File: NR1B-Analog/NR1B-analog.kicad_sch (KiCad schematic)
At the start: 64 parts, among them J8 Conn_01x04_Male, U1 DAC11001BPFBR, U10 LT3042MPMSE-PBF, U11 LDK320ADU120R, U12 20K, U13 OPA2189IDR, U14 DAC11001BPFBR, U2 ADR444ARZ, U3 OPA189IDGKT, U4 OPA2189IDR, U7 LT3093EMSE-PBF, U8 20K, U9 10K

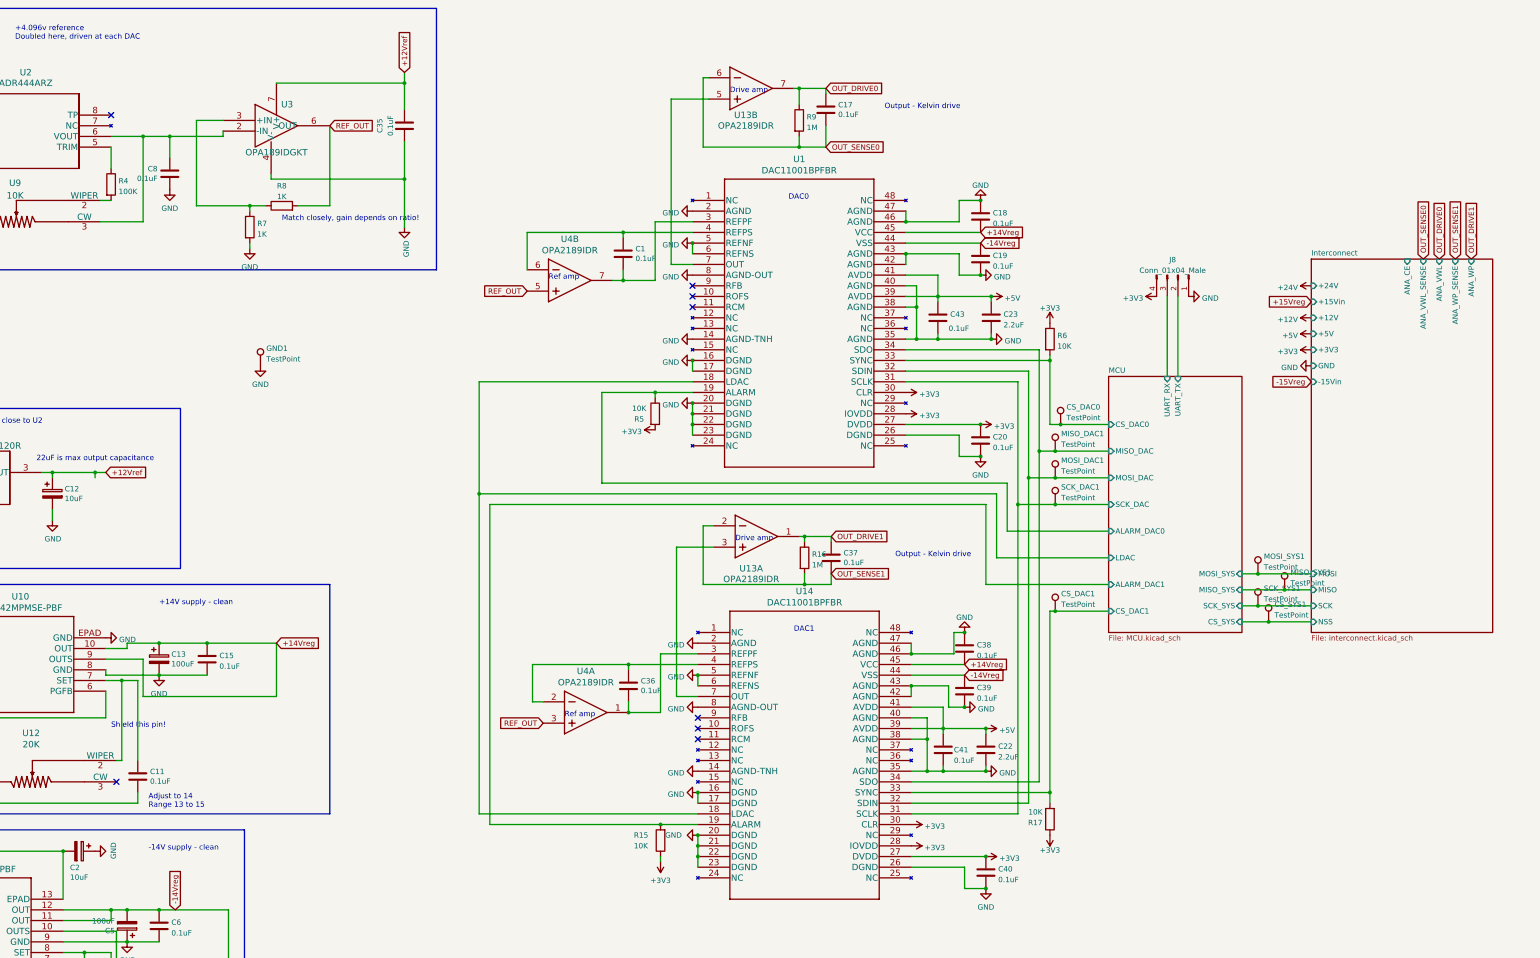
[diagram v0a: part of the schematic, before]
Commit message: Added ADC for voltage reading
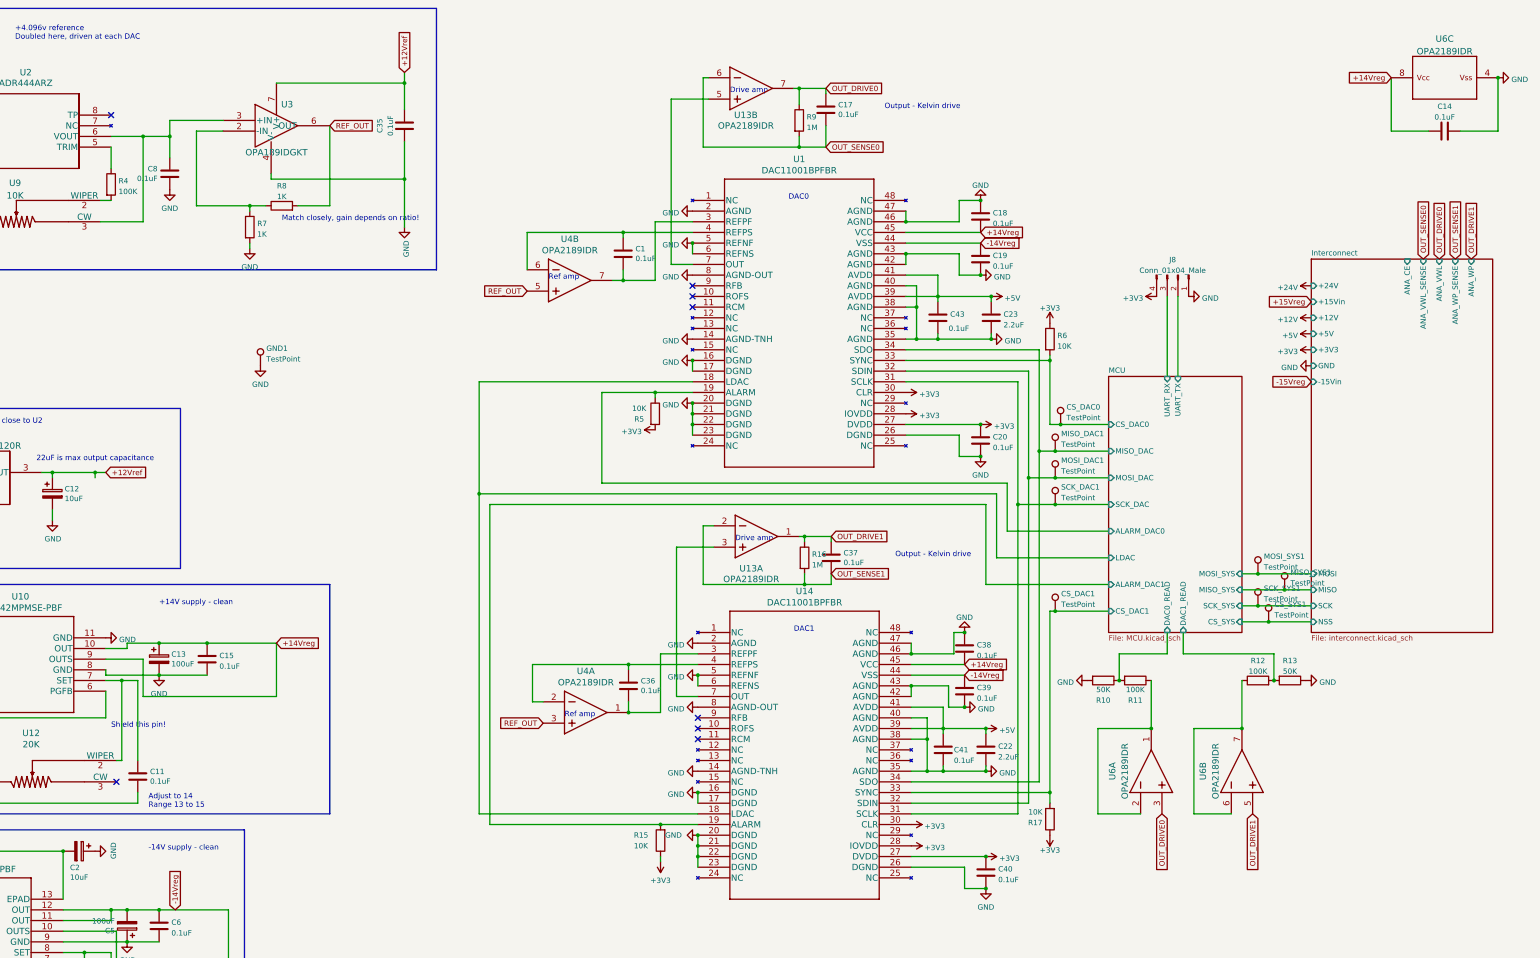
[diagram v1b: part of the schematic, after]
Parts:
- added C14: 0.1uF, Capacitor_SMD:C_0603_1608Metric, symbol Device:C
- added R10, R13: 50K, Resistor_SMD:R_0603_1608Metric, symbol Device:R
- added R11, R12: 100K, Resistor_SMD:R_0603_1608Metric, symbol Device:R
- added U6: OPA2189IDR, Package_SO:VSSOP-8_3.0x3.0mm_P0.65mm, symbol 2022-06-28_19-20-58:OPA2189IDR
- U1, U14: footprint PQFP48_DAC11001_TEX -> Package_QFP:TQFP-48_7x7mm_P0.5mm
- U10: footprint LT3042MPMSE-PBF_ADI -> Package_SO:MSOP-10-1EP_3x3mm_P0.5mm_EP1.68x1.88mm
- U11: footprint SOT-89_STM -> Package_TO_SOT_SMD:SOT-89-3
- U12, U8, U9: footprint SOT_3224J_BRN -> 3224J-1-103E:3224J-1-103E
- U13, U4: footprint D0008A_N -> Package_SO:VSSOP-8_3.0x3.0mm_P0.65mm
- U2: footprint R_8_ADI -> Package_SO:SO-8_3.9x4.9mm_P1.27mm
- U3: footprint DGK8_TEX -> Package_SO:VSSOP-8_3.0x3.0mm_P0.65mm
- U7: footprint LT3093EMSE-PBF_ADI -> Package_SO:MSOP-12-1EP_3x4mm_P0.65mm_EP1.65x2.85mm
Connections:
- net +14Vreg: now also C14.1, U6.8 (V+)
- net GND: now also U10.11 (GND), C14.2, R10.2, R13.1, U6.4 (V-); no longer U10.EPAD (GND)
- net OUT_DRIVE0: now also U6.3 (IN+)
- net OUT_DRIVE1: now also U6.5 (IN+)
- net at C8.1, U2.6 (VOUT), U9.3 (CW): now also U3.3 (+IN); no longer U3.2 (-IN)
- net at R7.1, R8.1: now also U3.2 (-IN); no longer U3.3 (+IN)
- new net: R11.1, U6.1 (OUT), U6.2 (IN-)
- new net: R12.1, U6.6 (IN-), U6.7 (OUT)
- new net MCU/DAC0_READ: R10.1, R11.2
- new net MCU/DAC1_READ: R12.2, R13.2
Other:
- sheet MCU ports: added DAC0_READ, DAC1_READ; removed none

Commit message: Fixed symbol libs, see notes from July 25 on PCB and schema
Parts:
- removed C41, C43: 0.1uF, Capacitor_SMD:C_0603_1608Metric, symbol Device:C
- added R18, R19: 47, Resistor_SMD:R_0603_1608Metric, symbol Device:R
- J8: value Conn_01x04_Male -> UART
- R10, R13: value 50K -> 47K
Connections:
- net MCU/DAC1_READ: now also R12.1; no longer R12.2
- net MCU/MISO_DAC: now also R18.2, R19.1; no longer U1.34 (SDO), U14.34 (SDO)
- net at U6.6 (IN-), U6.7 (OUT): now also R12.2; no longer R12.1
- new net: R18.1, U1.34 (SDO)
- new net: R19.2, U14.34 (SDO)
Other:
- sheet Interconnect ports: added ACK, ERROR; removed ANA_CE
- sheet MCU ports: added ACK, ERROR; removed none
- note added: "7/25/2022"
- note added: "ADC amp"
- note added: "Adjust to -14 range -13 to -15"
- note added: "Match R7 and R8 closely, gain depends on ratio!"
- note added: "NR1B-Analog"
- note added: "v1.0"
- note removed: "Adjust for -14 exactly range -13 to -15"
- note removed: "Match closely, gain depends on ratio!"
- note removed: "Shield this pin!"
- moved on the sheet: C10, C12, C14, C22, C23, CS_DAC1, CS_SYS1, GND1, MISO_SYS1, MOSI_SYS1, R10, R11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

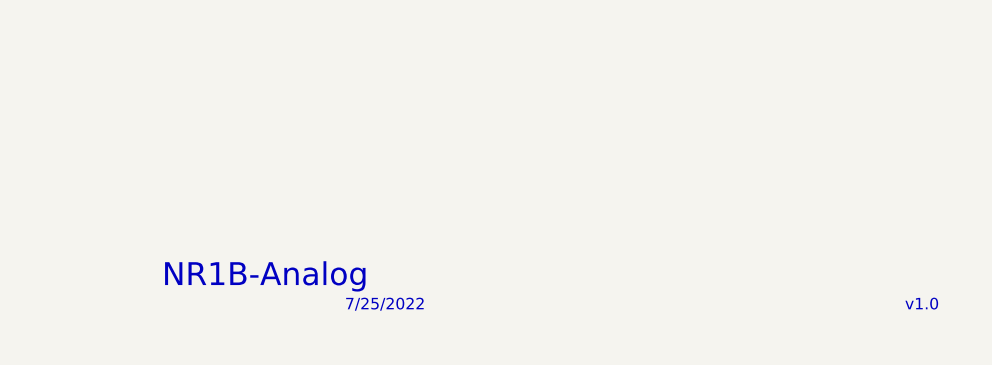
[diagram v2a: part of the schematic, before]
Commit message: Labeled sheets, adjusted pot location
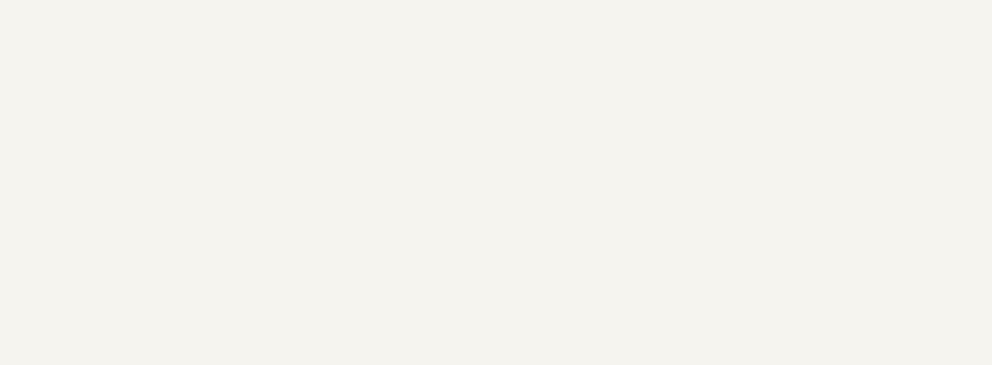
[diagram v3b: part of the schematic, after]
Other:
- note removed: "7/25/2022"
- note removed: "NR1B-Analog"
- note removed: "v1.0"
- company: (none) -> University of Dallas
- title: (none) -> NR1B-Analog
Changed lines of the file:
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@@
 (kicad_sch (version 20211123) (generator eeschema)
   (paper "USLedger")
+  (title_block
+    (title "NR1B-Analog")
+    (date "2022-07-26")
+    (rev "v1.0")
+    (company "University of Dallas")
+    (comment 1 "Isaac Kelly")
+  )
   (junction (at 25.4 227.33) (diameter 0) (color 0 0 0 0)
   )
@@
     (effects (font (size 1.27 1.27)) (justify left bottom))
   )
-  (text "v1.0" (at 403.86 262.89 0)
-    (effects (font (size 1.27 1.27)) (justify left bottom))
-  )
   (text "Adjust to 14\nRange 13 to 15" (at 91.44 203.2 0)
     (effects (font (size 1.27 1.27)) (justify left bottom))
@@
     (effects (font (size 1.27 1.27)) (justify left bottom))
   )
-  (text "7/25/2022" (at 341.63 262.89 0)
-    (effects (font (size 1.27 1.27)) (justify left bottom))
-  )
   (text "Ref amp" (at 186.69 77.47 0)
     (effects (font (size 1.27 1.27)) (justify left bottom))
@@
     (effects (font (size 1.27 1.27)) (justify left bottom))
   )
-  (text "NR1B-Analog" (at 321.31 260.35 0)
-    (effects (font (size 2.54 2.54)) (justify left bottom))
-  )
   (text "Adjust to -14\nrange -13 to -15" (at 83.82 262.89 0)

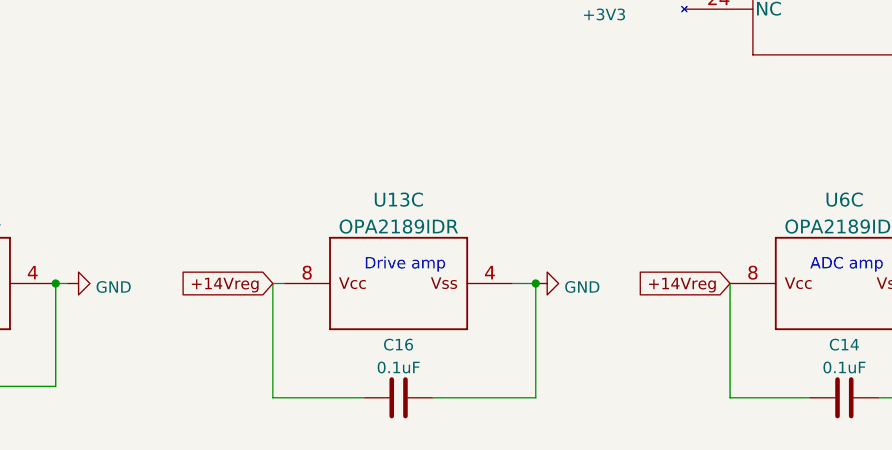
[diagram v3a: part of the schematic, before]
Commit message: 12v supply to dual op-amps
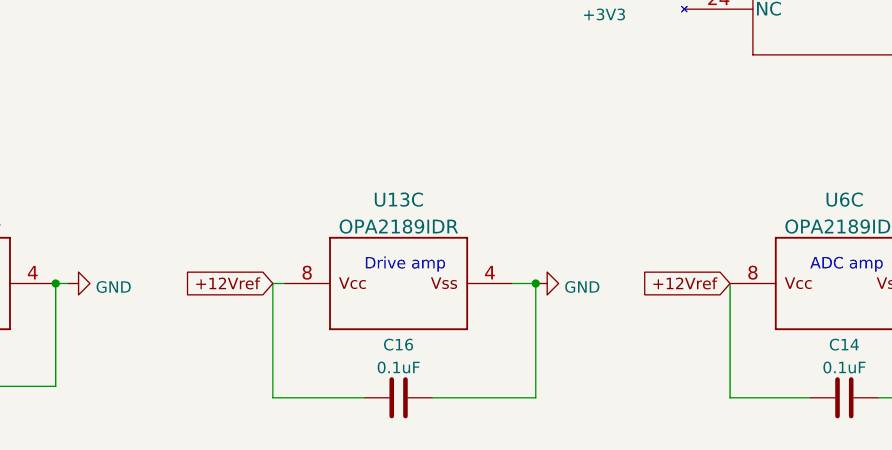
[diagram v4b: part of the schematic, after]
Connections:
- net +12Vref: now also C14.1, C16.1, U13.8 (V+), U6.8 (V+)
- net +14Vreg: no longer C14.1, C16.1, U13.8 (V+), U6.8 (V+)
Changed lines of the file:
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@@
-    )
-  )
-  (global_label "+14Vreg" (shape input) (at 176.53 250.19 180) (fields_autoplaced)
-    (effects (font (size 1.27 1.27)) (justify right))
-    (property "Intersheet References" "${INTERSHEET_REFS}" (id 0) (at 166.102 250.2694 0)
-      (effects (font (size 1.27 1.27)) (justify right) hide)
     )
   )
@@
     (property "Intersheet References" "${INTERSHEET_REFS}" (id 0) (at 266.9075 45.6406 0)
       (effects (font (size 1.27 1.27)) (justify left) hide)
+    )
+  )
+  (global_label "+12Vref" (shape input) (at 227.33 250.19 180) (fields_autoplaced)
+    (effects (font (size 1.27 1.27)) (justify right))
+    (property "Intersheet References" "${INTERSHEET_REFS}" (id 0) (at 217.3253 250.1106 0)
+      (effects (font (size 1.27 1.27)) (justify right) hide)
     )
   )
@@
     (property "Intersheet References" "${INTERSHEET_REFS}" (id 0) (at 145.048 40.5606 0)
       (effects (font (size 1.27 1.27)) (justify left) hide)
-    )
-  )
-  (global_label "+14Vreg" (shape input) (at 227.33 250.19 180) (fields_autoplaced)
-    (effects (font (size 1.27 1.27)) (justify right))
-    (property "Intersheet References" "${INTERSHEET_REFS}" (id 0) (at 216.902 250.1106 0)
-      (effects (font (size 1.27 1.27)) (justify right) hide)
     )
   )
@@
     )
   )
+  (global_label "+12Vref" (shape input) (at 176.53 250.19 180) (fields_autoplaced)
+    (effects (font (size 1.27 1.27)) (justify right))
+    (property "Intersheet References" "${INTERSHEET_REFS}" (id 0) (at 166.5253 250.1106 0)
+      (effects (font (size 1.27 1.27)) (justify right) hide)
+    )
+  )

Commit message: BOM, fiducials
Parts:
- added FID1, FID2, FID3: Fiducial, Fiducial:Fiducial_0.5mm_Mask1.5mm, symbol Mechanical:Fiducial
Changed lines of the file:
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@@
     (pin "1")
+  )
+  (symbol (lib_id "Mechanical:Fiducial") (at 369.57 33.02 0) (unit 1)
+    (in_bom yes) (on_board yes) (fields_autoplaced)
+    (property "Reference" "FID2" (id 0) (at 371.729 32.1853 0)
+      (effects (font (size 1.27 1.27)) (justify left))
+    )
+    (property "Value" "Fiducial" (id 1) (at 371.729 34.7222 0)
+      (effects (font (size 1.27 1.27)) (justify left))
+    )
+    (property "Footprint" "Fiducial:Fiducial_0.5mm_Mask1.5mm" (id 2) (at 369.57 33.02 0)
+      (effects (font (size 1.27 1.27)) hide)
+    )
+    (property "Datasheet" "~" (id 3) (at 369.57 33.02 0)
+      (effects (font (size 1.27 1.27)) hide)
+    )
   )
   (symbol (lib_id "Device:C") (at 289.56 115.57 0) (unit 1)
@@
     (pin "8")
   )
+  (symbol (lib_id "Mechanical:Fiducial") (at 369.57 22.86 0) (unit 1)
+    (in_bom yes) (on_board yes) (fields_autoplaced)
+    (property "Reference" "FID1" (id 0) (at 371.729 22.0253 0)
+      (effects (font (size 1.27 1.27)) (justify left))
+    )
+    (property "Value" "Fiducial" (id 1) (at 371.729 24.5622 0)
+      (effects (font (size 1.27 1.27)) (justify left))
+    )
+    (property "Footprint" "Fiducial:Fiducial_0.5mm_Mask1.5mm" (id 2) (at 369.57 22.86 0)
+      (effects (font (size 1.27 1.27)) hide)
+    )
+    (property "Datasheet" "~" (id 3) (at 369.57 22.86 0)
+      (effects (font (size 1.27 1.27)) hide)
+    )
+  )
   (symbol (lib_id "Device:C") (at 289.56 62.23 0) (unit 1)
     (in_bom yes) (on_board yes) (fields_autoplaced)
@@
     )
     (pin "1")
+  )
+  (symbol (lib_id "Mechanical:Fiducial") (at 369.57 43.18 0) (unit 1)
+    (in_bom yes) (on_board yes) (fields_autoplaced)
+    (property "Reference" "FID3" (id 0) (at 371.729 42.3453 0)
+      (effects (font (size 1.27 1.27)) (justify left))
+    )
+    (property "Value" "Fiducial" (id 1) (at 371.729 44.8822 0)
+      (effects (font (size 1.27 1.27)) (justify left))
+    )
+    (property "Footprint" "Fiducial:Fiducial_0.5mm_Mask1.5mm" (id 2) (at 369.57 43.18 0)
+      (effects (font (size 1.27 1.27)) hide)
+    )
+    (property "Datasheet" "~" (id 3) (at 369.57 43.18 0)
+      (effects (font (size 1.27 1.27)) hide)
+    )
   )
   (symbol (lib_id "power:GND") (at 96.52 55.88 0) (unit 1)
@@
       (reference "FB3") (unit 1) (value "FerriteBead") (footprint "Inductor_SMD:L_0805_2012Metric")
     )
+    (path "/a156e368-5eaa-4055-885b-4dc6a9421257"
+      (reference "FID1") (unit 1) (value "Fiducial") (footprint "Fiducial:Fiducial_0.5mm_Mask1.5mm")
+    )
+    (path "/75a6e213-de52-4f99-93dc-2e97dfd7dafa"
+      (reference "FID2") (unit 1) (value "Fiducial") (footprint "Fiducial:Fiducial_0.5mm_Mask1.5mm")
+    )
+    (path "/abf288d1-2057-41b6-a678-d28b983d7fd8"
+      (reference "FID3") (unit 1) (value "Fiducial") (footprint "Fiducial:Fiducial_0.5mm_Mask1.5mm")
+    )
     (path "/04181750-5cf6-4122-b89d-e16ab9ca9019"

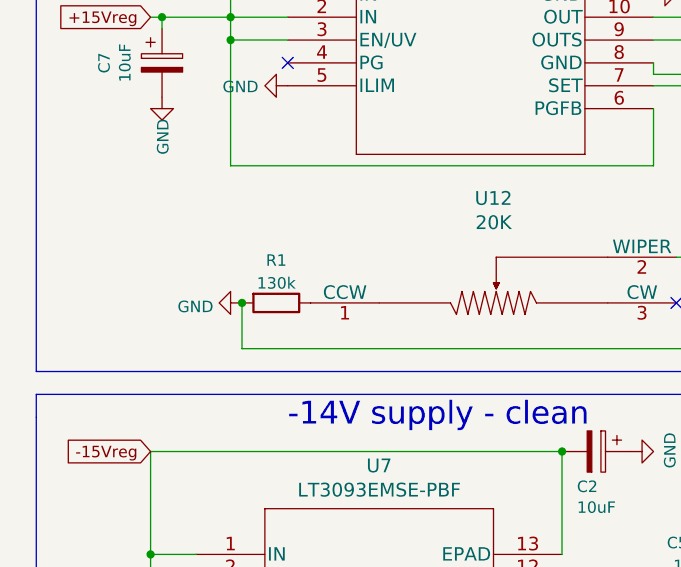
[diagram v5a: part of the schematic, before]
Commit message: BOM drafted, fixed R1 value
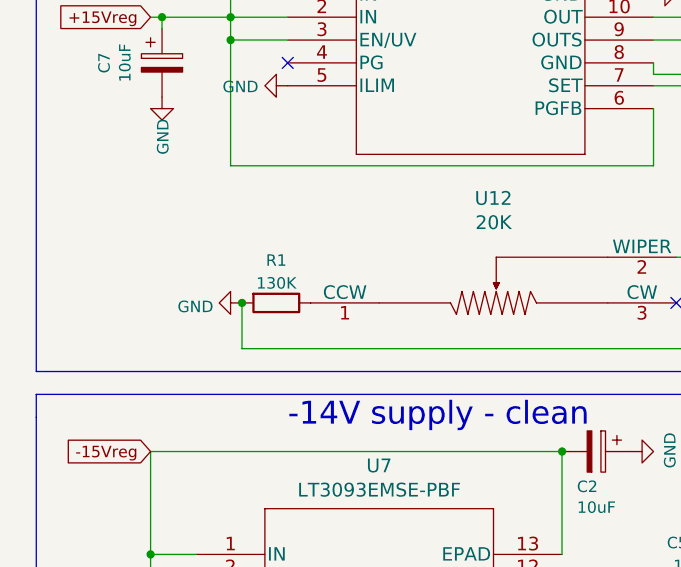
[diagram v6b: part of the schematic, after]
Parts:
- R1: value 130k -> 130K
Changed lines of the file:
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@@
     (in_bom yes) (on_board yes) (fields_autoplaced)
     (property "Reference" "R1" (id 0) (at 39.37 192.1342 90))
-    (property "Value" "130k" (id 1) (at 39.37 194.6711 90))
+    (property "Value" "130K" (id 1) (at 39.37 194.6711 90))
     (property "Footprint" "Resistor_SMD:R_0603_1608Metric" (id 2) (at 39.37 195.072 90)
       (effects (font (size 1.27 1.27)) hide)
@@
     )
     (path "/00000000-0000-0000-0000-000062c027ab"
-      (reference "R1") (unit 1) (value "130k") (footprint "Resistor_SMD:R_0603_1608Metric")
+      (reference "R1") (unit 1) (value "130K") (footprint "Resistor_SMD:R_0603_1608Metric")
     )
     (path "/00000000-0000-0000-0000-000062c127fe"

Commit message: Cap footprints adjusted for size constraints
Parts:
- C13, C5: footprint Capacitor_SMD:CP_Elec_5x5.3 -> Capacitor_SMD:CP_Elec_6.3x5.8
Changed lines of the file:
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@@
       (effects (font (size 1.27 1.27)) (justify left))
     )
-    (property "Footprint" "Capacitor_SMD:CP_Elec_5x5.3" (id 2) (at 94.9452 171.45 0)
+    (property "Footprint" "Capacitor_SMD:CP_Elec_6.3x5.8" (id 2) (at 94.9452 171.45 0)
       (effects (font (size 1.27 1.27)) hide)
     )
@@
       (effects (font (size 1.27 1.27)) (justify left))
     )
-    (property "Footprint" "Capacitor_SMD:CP_Elec_5x5.3" (id 2) (at 85.3948 227.33 0)
+    (property "Footprint" "Capacitor_SMD:CP_Elec_6.3x5.8" (id 2) (at 85.3948 227.33 0)
       (effects (font (size 1.27 1.27)) hide)
     )
@@
     )
     (path "/00000000-0000-0000-0000-000062c185ba"
-      (reference "C5") (unit 1) (value "100uF") (footprint "Capacitor_SMD:CP_Elec_5x5.3")
+      (reference "C5") (unit 1) (value "100uF") (footprint "Capacitor_SMD:CP_Elec_6.3x5.8")
     )
     (path "/5fc3b5f2-c211-40a5-af34-b74f43ba1340"
@@
     )
     (path "/00000000-0000-0000-0000-000062c06aa1"
-      (reference "C13") (unit 1) (value "100uF") (footprint "Capacitor_SMD:CP_Elec_5x5.3")
+      (reference "C13") (unit 1) (value "100uF") (footprint "Capacitor_SMD:CP_Elec_6.3x5.8")
     )
     (path "/603e504c-edb3-4de2-87d8-d6fe59535435"
